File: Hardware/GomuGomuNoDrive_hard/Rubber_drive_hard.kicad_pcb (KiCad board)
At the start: 2 copper layers, 89 x 75 mm, 67 parts, among them J1 9V, J2 AudioJack3, J3 AudioJack3, J4 Conn_02x03_Counter_Clockwise, Q10 BC550, Q4 BS170, Q5 BS170, Q9 BC550, SW1 SW_DPDT_x2, SW10 SW_DPDT_x2, SW11 SW_SPDT, SW2 SW_DPDT_x2, SW3 SW_DPDT_x2, SW4 SW_DPDT_x2, SW5 SW_SPDT_MSM, SW6 SW_SPDT_MSM, SW7 SW_DPDT_x2, SW8 SW_DPDT_x2, U2 TC7662Bx0A, U5 TL074

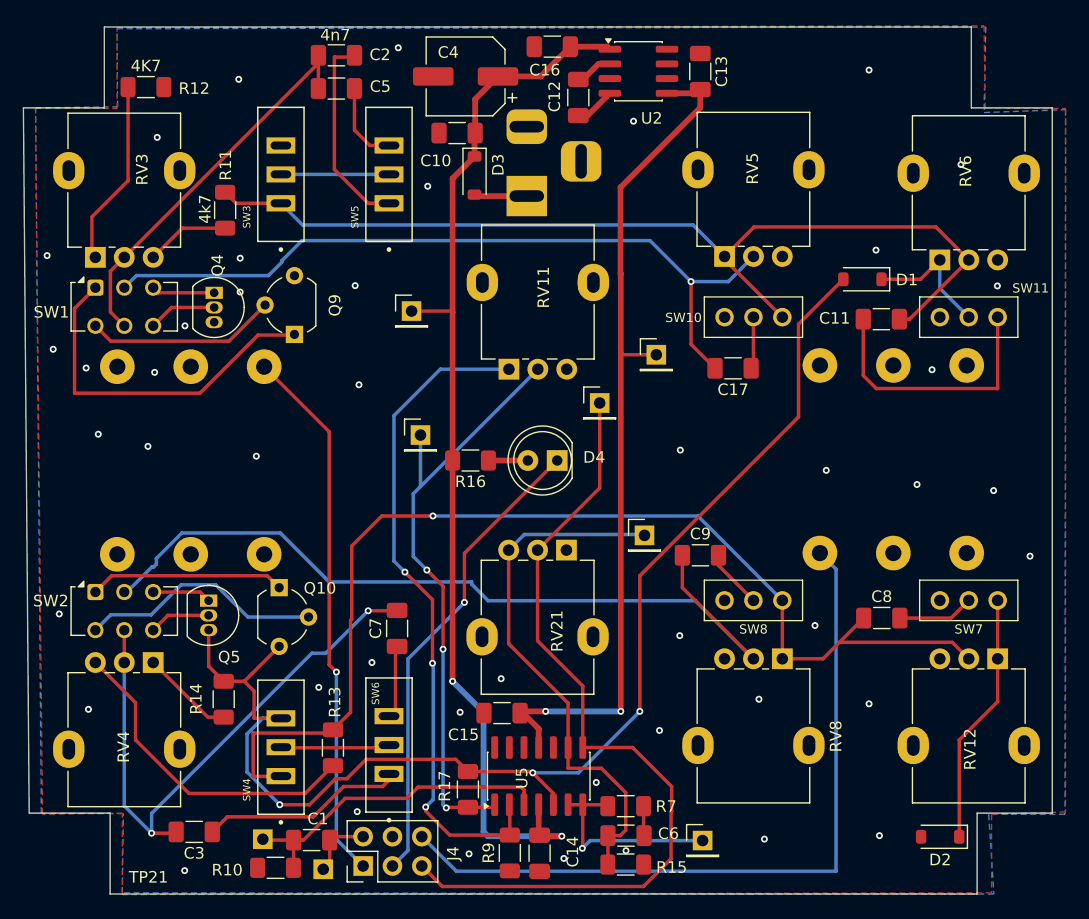
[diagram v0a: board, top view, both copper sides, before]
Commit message: Correct Schematic/PCB for Hard clip pedal
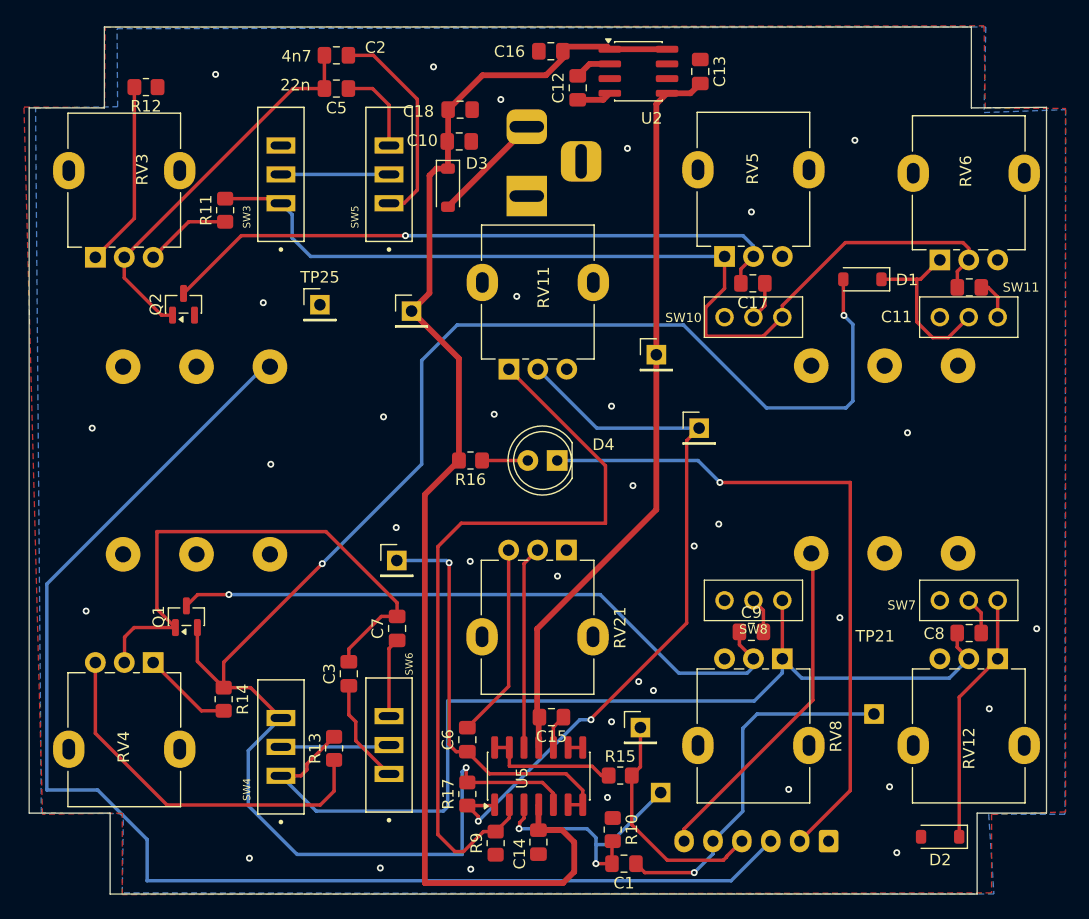
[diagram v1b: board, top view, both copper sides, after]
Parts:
- removed C4: 47u, Capacitor_SMD:CP_Elec_6.3x5.4
- removed J4: Conn_02x03_Counter_Clockwise, Connector_PinHeader_2.54mm:PinHeader_2x03_P2.54mm_Vertical
- removed Q10, Q9: BC550, Package_TO_SOT_THT:TO-92_Wide
- removed Q4, Q5: BS170, Package_TO_SOT_THT:TO-92_Inline
- removed R7: 10K, Resistor_SMD:R_1206_3216Metric_Pad1.30x1.75mm_HandSolder
- removed SW1, SW2: SW_DPDT_x2, Button_Switch_THT:SW_CK_JS202011CQN_DPDT_Straight
- added C18: 10u, Capacitor_SMD:C_0805_2012Metric_Pad1.18x1.45mm_HandSolder, F.Cu at (49.3, 19.9)
- added J5: Conn_01x06_Socket, Connector_JST:JST_EH_B6B-EH-A_1x06_P2.50mm_Vertical, B.Cu at (81.2, 83.2)
- added Q1: BC850, Package_TO_SOT_SMD:SOT-23, F.Cu at (25.6, 63.8)
- added Q2: BC850, Package_TO_SOT_SMD:SOT-23, F.Cu at (25.4, 36.7)
- C1: value C -> 22n - film; footprint Capacitor_SMD:C_1206_3216Metric_Pad1.33x1.80mm_HandSolder -> Capacitor_SMD:C_0805_2012Metric_Pad1.18x1.45mm_HandSolder
- C10, C11, C12, C13, C14, C15, C16, C17, C2, C5, C8, C9: footprint Capacitor_SMD:C_1206_3216Metric_Pad1.33x1.80mm_HandSolder -> Capacitor_SMD:C_0805_2012Metric_Pad1.18x1.45mm_HandSolder
- C3: value 10n -> 4n7; footprint Capacitor_SMD:C_1206_3216Metric_Pad1.33x1.80mm_HandSolder -> Capacitor_SMD:C_0805_2012Metric_Pad1.18x1.45mm_HandSolder
- C6: value C -> 220n; footprint Capacitor_SMD:C_1206_3216Metric_Pad1.33x1.80mm_HandSolder -> Capacitor_SMD:C_0805_2012Metric_Pad1.18x1.45mm_HandSolder
- C7: value 10n -> 22n; footprint Capacitor_SMD:C_1206_3216Metric_Pad1.33x1.80mm_HandSolder -> Capacitor_SMD:C_0805_2012Metric_Pad1.18x1.45mm_HandSolder
- D1: value BAT42W -> C8598
- D2: value BAT41 -> C8598
- D3: value 1N5818 -> C8598
- R10, R11, R13, R16, R17: footprint Resistor_SMD:R_1206_3216Metric_Pad1.30x1.75mm_HandSolder -> Resistor_SMD:R_0805_2012Metric_Pad1.20x1.40mm_HandSolder
- R12, R14: value 4K7 -> 100; footprint Resistor_SMD:R_1206_3216Metric_Pad1.30x1.75mm_HandSolder -> Resistor_SMD:R_0805_2012Metric_Pad1.20x1.40mm_HandSolder
- R15: value 1M -> 100; footprint Resistor_SMD:R_1206_3216Metric_Pad1.30x1.75mm_HandSolder -> Resistor_SMD:R_0805_2012Metric_Pad1.20x1.40mm_HandSolder
- R9: value R -> 6K8; footprint Resistor_SMD:R_1206_3216Metric_Pad1.30x1.75mm_HandSolder -> Resistor_SMD:R_0805_2012Metric_Pad1.20x1.40mm_HandSolder
- RV11: value R_Potentiometer -> 100K_Log
- RV12, RV5, RV6, RV8: value 100? -> 5K
- RV21: value 1M -> 100K Log
- TP25: value post_diode_DC -> GND
- U5: value TL074 -> OPA1679
- moved TP21 49.5 mm to (85.1, 72.2)
- moved TP24 35.9 mm to (43.8, 58.9)
- moved TP22 34.7 mm to (66.6, 79.0)
- moved TP25 34.4 mm to (37.1, 36.8)
- moved R10 29.4 mm to (62.5, 82.2), turned to -90 degrees
- moved TP26 28.3 mm to (64.9, 73.3)
- moved C1 27.1 mm to (63.5, 85.1)
- moved TP23 24.1 mm to (70.0, 47.5)
- moved C3 19.1 mm to (39.6, 68.7), turned to 90 degrees
- moved C6 16.0 mm to (49.9, 74.4), turned to 90 degrees
- moved C11 8.09 mm to (93.3, 35.3), turned to 180 degrees
- moved C9 7.96 mm to (74.5, 65.1)
- moved R15 7.71 mm to (63.1, 77.5), turned to 0 degrees
- moved C8 7.67 mm to (93.3, 65.2)
- moved C17 7.55 mm to (74.6, 34.9)
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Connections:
- C6 pad 1: Net-(C6-Pad1) -> Net-(U5B--)
- C6 pad 2: Net-(U5C--) -> Net-(C6-Pad2)
- J1 pad 1: V -> GND
- J1 pad 2: GND -> V
- R15 pad 1: GND -> Net-(U5D--)
- R15 pad 2: Net-(U5C--) -> out
- RV21 pad 1: unconnected-(RV21-Pad1) -> GND
- RV21 pad 2: out -> Net-(U5D-+)
- RV21 pad 3: Net-(U5C--) -> Net-(C6-Pad2)
- TP25 pad 1: Net-(U5C--) -> GND
- U2 pad 8: unconnected-(U2-V+-Pad8) -> 9V
- U5 pad 12: unconnected-(U5D-+-Pad12) -> Net-(U5D-+)
- U5 pad 13: unconnected-(U5D---Pad13) -> Net-(U5D--)
- U5 pad 14: unconnected-(U5-Pad14) -> Net-(U5D--)
- U5 pad 8: out -> Net-(U5C--)
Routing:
- net JackInput_tip: track 46.7 -> 114.3 mm, vias 1 -> 0
- net out: track 72.3 -> 20.2 mm
- net Net-(U5C--): track 46.7 -> 1.27 mm
- net Rubber_hard_north: track 111.4 -> 147.3 mm
- net JackOutput_tip: track 65.2 -> 29.7 mm
- net Net-(Q9-C): track 31.0 -> 0.00 mm
- net CircuitInput: track 5.77 -> 31.4 mm, vias 0 -> 1
- net Net-(Q10-B): track 21.2 -> 0.00 mm
- net 9V: track 94.1 -> 115.2 mm, vias 2 -> 0
- net Net-(SW11-C): track 23.1 -> 3.52 mm
- net LED_CATHODE: track 41.0 -> 59.1 mm
- net Net-(U5B--): track 18.0 -> 36.0 mm
- net Net-(U5D-+): track 0.00 -> 17.6 mm
- net Net-(Q1-C): track 73.0 -> 56.0 mm, vias 0 -> 1
- net Net-(Q10-C): track 16.9 -> 0.00 mm
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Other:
- board size 89 x 75 mm -> 88 x 75 mm
- board text added: "22n"
- board text added: "4n7"
